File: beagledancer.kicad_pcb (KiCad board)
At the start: 2 copper layers, 40.6 x 29.2 mm, 12 parts, among them P9 BeagleBone, Q1 12MHz, U1 MAX3421

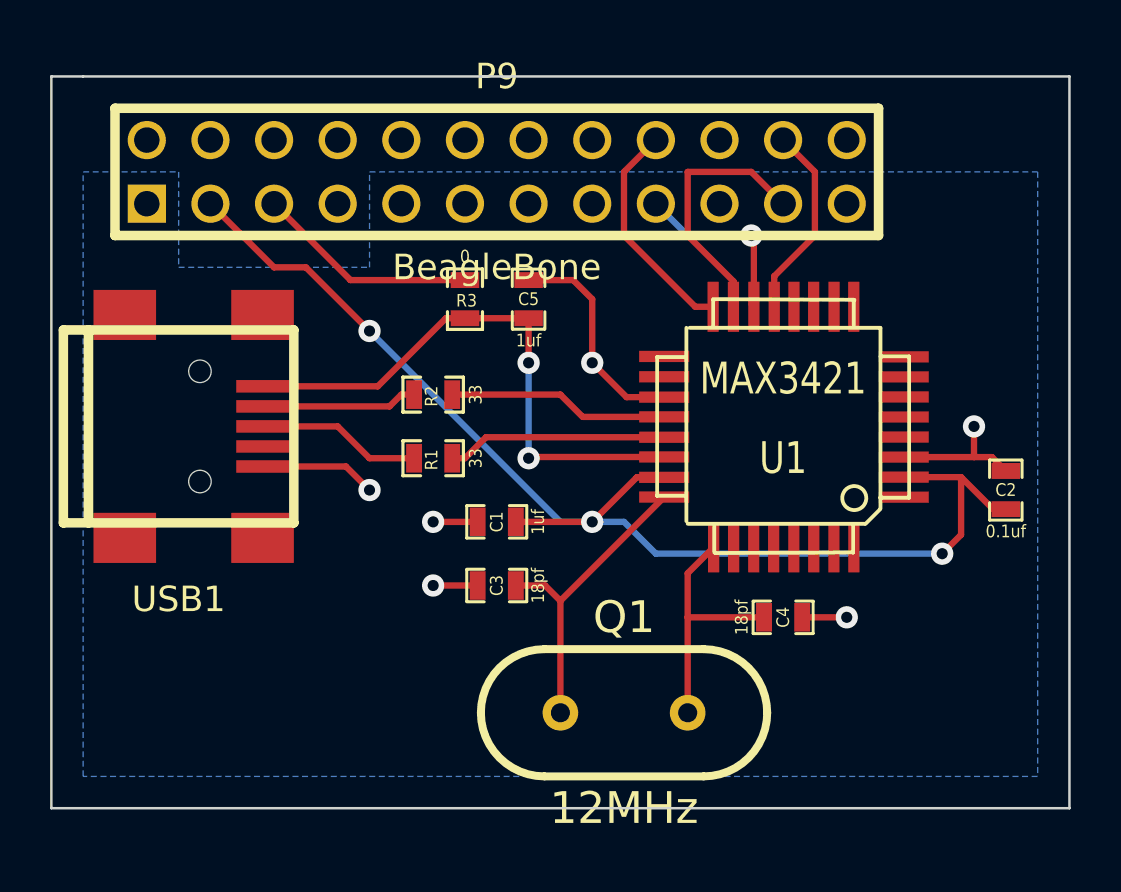
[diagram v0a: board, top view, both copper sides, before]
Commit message: Update based on feedback from Michael Ossmann (mossmann)
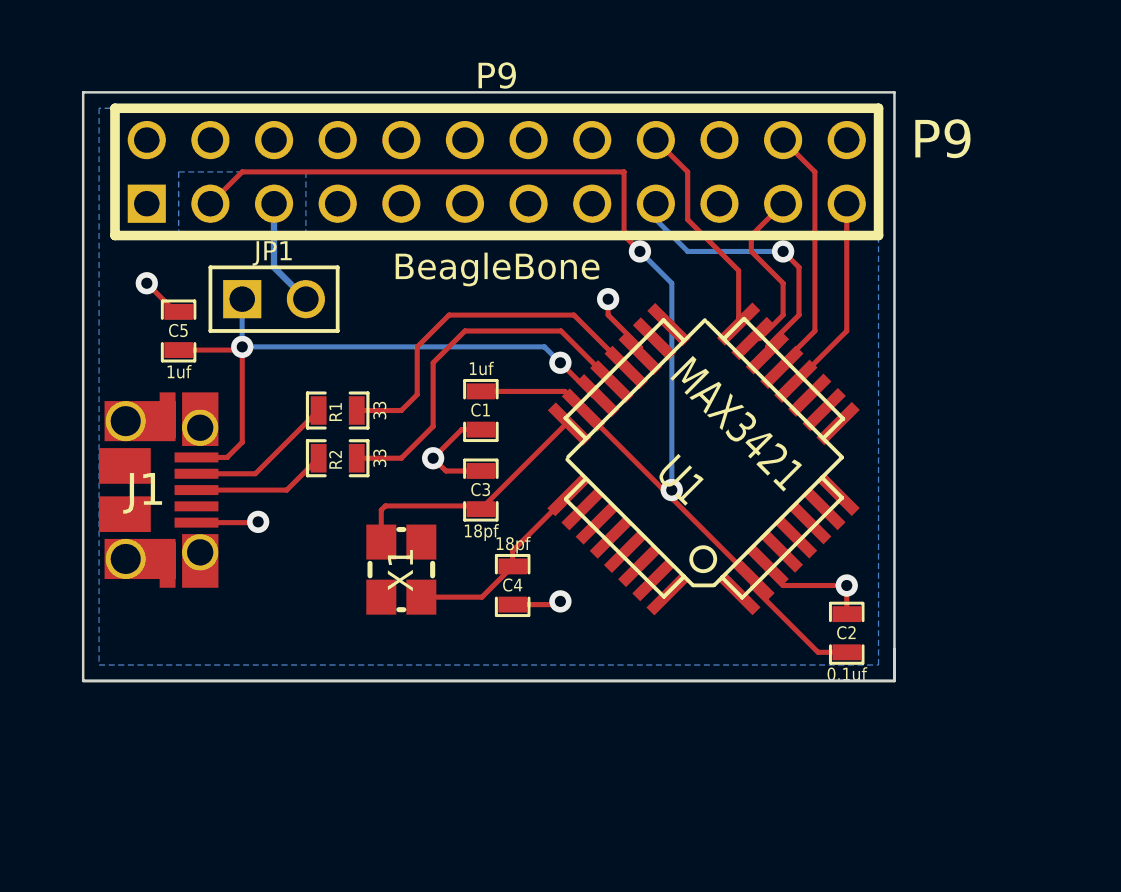
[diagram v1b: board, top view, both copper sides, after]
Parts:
- removed Q1: 12MHz, HC-49V
- removed R3: 0, SM0603_Resistor
- removed USB1: USB-MINI-B, USB_MINI_B
- added J1: USB-MICRO-B, GSG-USB-MICROB-FCI-10103594, F.Cu at (198.1, 152.4)
- added JP1: JUMPER, PIN_ARRAY_2X1, F.Cu at (205.7, 144.8)
- added X1: XTAL4PIN, GSG-XTAL3.2x2.5mm, F.Cu at (210.8, 155.6)
- moved C5 14.0 mm to (201.9, 146.1)
- moved C4 10.9 mm to (215.3, 156.2), turned to 270 degrees
- moved C2 8.54 mm to (228.6, 158.1)
- moved R2 4.58 mm to (208.3, 151.1)
- moved C1 4.49 mm to (214.0, 149.2), turned to 270 degrees
- moved R1 4.26 mm to (208.3, 149.2)
- moved C3 3.86 mm to (214.0, 152.4), turned to 90 degrees
- moved U1 3.42 mm to (222.9, 151.1), turned to 135 degrees
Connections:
- P9 pad 23: N-0000014 (its old number) -> N-0000038
- R1 pad 1: N-0000038 -> N-0000029
- R2 pad 1: N-0000029 -> N-0000027
- U1 pad 12: N-0000048 (its old number) -> N-0000038
- U1 pad 21: N-0000038 -> N-0000027
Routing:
- net N-0000027: track 0.00 -> 14.6 mm
- net GND: track 24.3 -> 18.1 mm
- net N-0000029: track 8.83 -> 14.3 mm
- net +5V: track 8.88 -> 4.34 mm
- net SPI0_CS0: track 7.37 -> 11.1 mm
- net SPI0_D0: track 10.5 -> 7.08 mm
- net N-0000049: track 22.7 -> 25.7 mm
- net SPI0_SCLK: track 7.85 -> 10.1 mm
- net N-000002: track 12.4 -> 10.2 mm
- net N-000003: track 10.1 -> 7.95 mm
- net N-0000038: track 8.81 -> 7.31 mm
- net N-0000025: track 6.14 -> 5.40 mm
- net N-0000022: track 6.47 -> 5.92 mm
- net +3.3V: track 49.6 -> 49.9 mm, vias 3 -> 2
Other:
- board size 40.6 x 29.2 mm -> 32.4 x 23.5 mm
- net class Default: clearance 0.254 -> 0.2032; trace_width 0.254 -> 0.2032
- rule trace_clearance: 0.254 -> 0.2032
- rule trace_min: 0.254 -> 0.2032
- board text added: "P9"

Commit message: Tweak layout to detect OTG pin status with GPIO pin
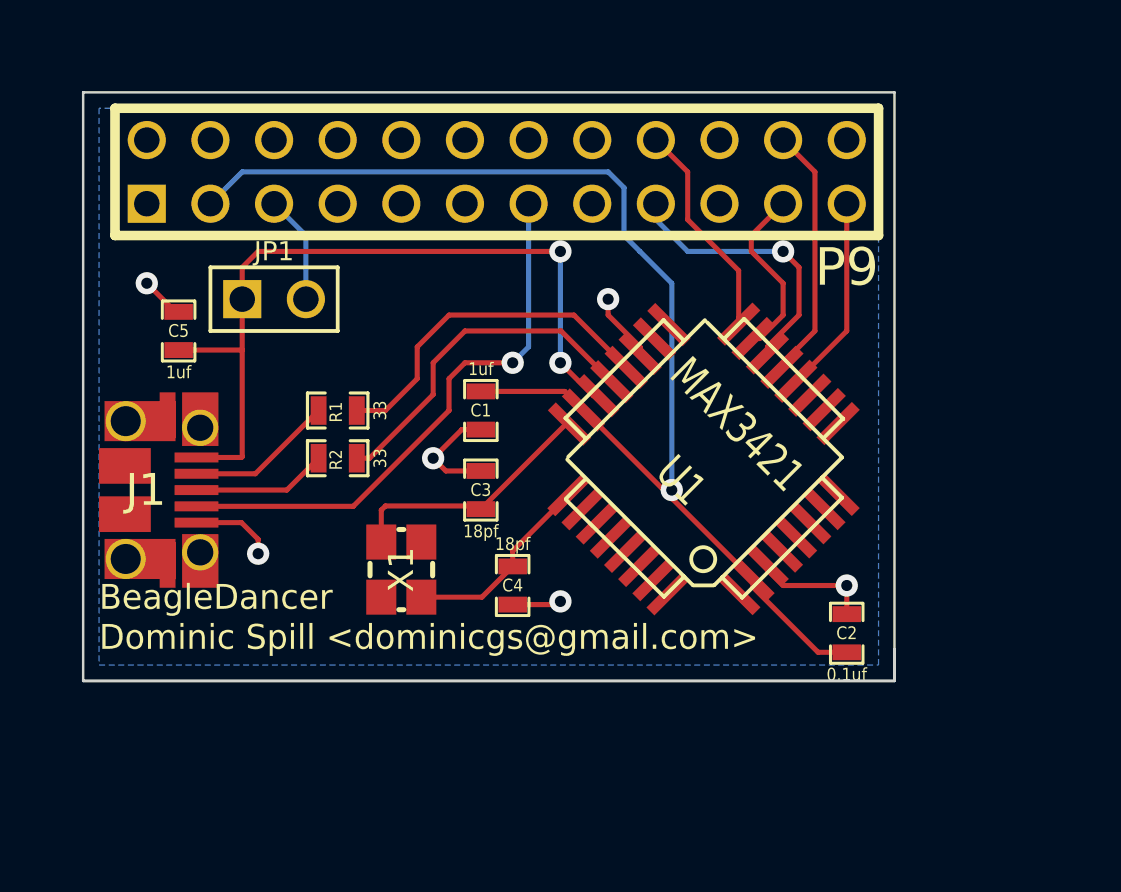
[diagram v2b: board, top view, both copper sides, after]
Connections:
- J1 pad 4: N-0000026 (its old number) -> USB_ID
- P9 pad 13: N-0000048 (its old number) -> USB_ID
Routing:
- net USB_ID: track 0.00 -> 22.4 mm, vias 0 -> 1
- net N-0000048: track 25.7 -> 31.6 mm
- net GND: track 18.1 -> 19.0 mm
- net N-0000025: track 14.6 -> 13.9 mm
- net +3.3V: track 49.9 -> 49.5 mm, vias 2 -> 1
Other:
- board text added: "BeagleDancer Dominic Spill <dominicgs@gmail.com>"

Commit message: More feedback
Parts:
- moved C3 4.84 mm to (209.6, 154.3), turned to 180 degrees
- moved X1 3.18 mm to (213.4, 153.7)
- moved C2 1.91 mm to (226.7, 158.1), turned to 0 degrees
- moved C4 1.42 mm to (216.5, 156.8), turned to 0 degrees
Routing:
- net GND: track 19.0 -> 13.7 mm, vias 6 -> 8
- net +3.3V: track 49.5 -> 48.3 mm, vias 1 -> 0
- net N-000002: track 10.2 -> 9.48 mm
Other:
- net class Default: via_dia 0.889 -> 1.016; via_drill 0.635 -> 0.508
- net class Power added: clearance 0.2032, trace_width 0.3048, via_dia 1.016, via_drill 0.508

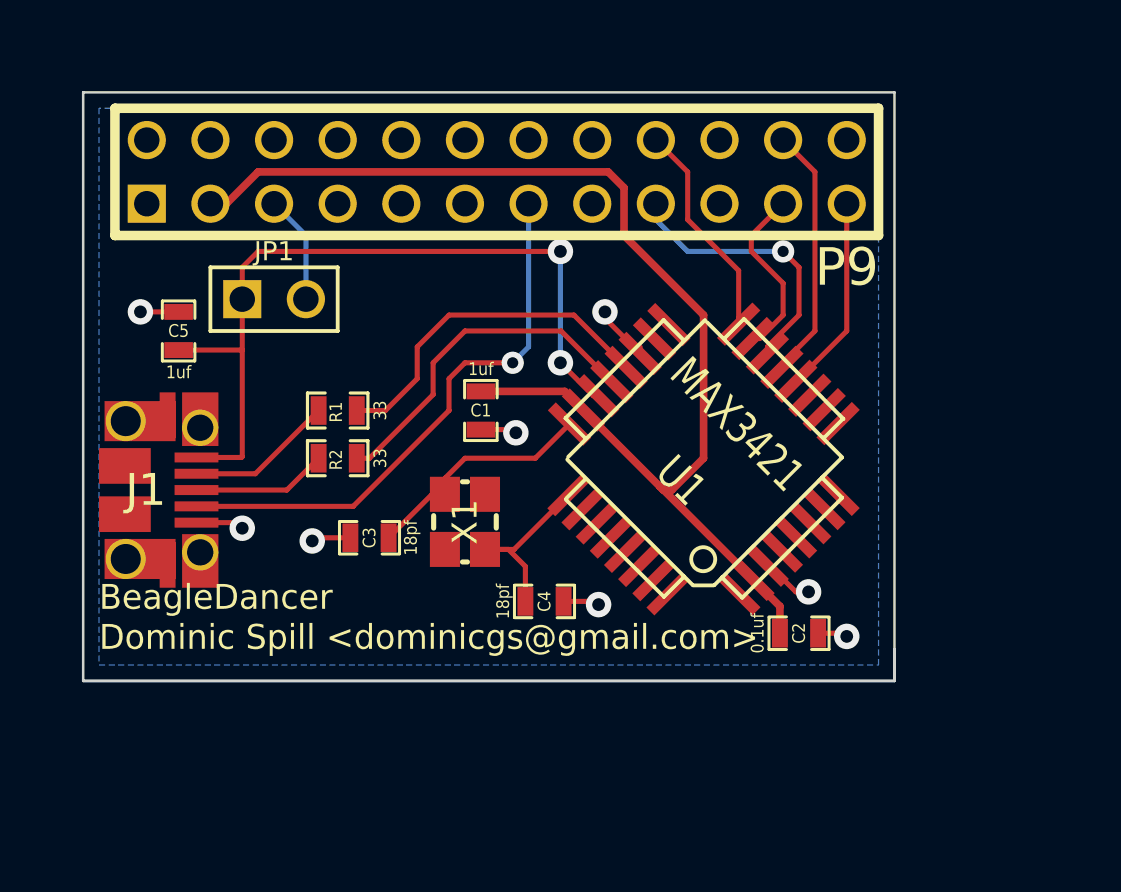
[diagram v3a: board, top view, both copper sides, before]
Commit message: Connect INT and GPX to GPIO pins on the Beagle.
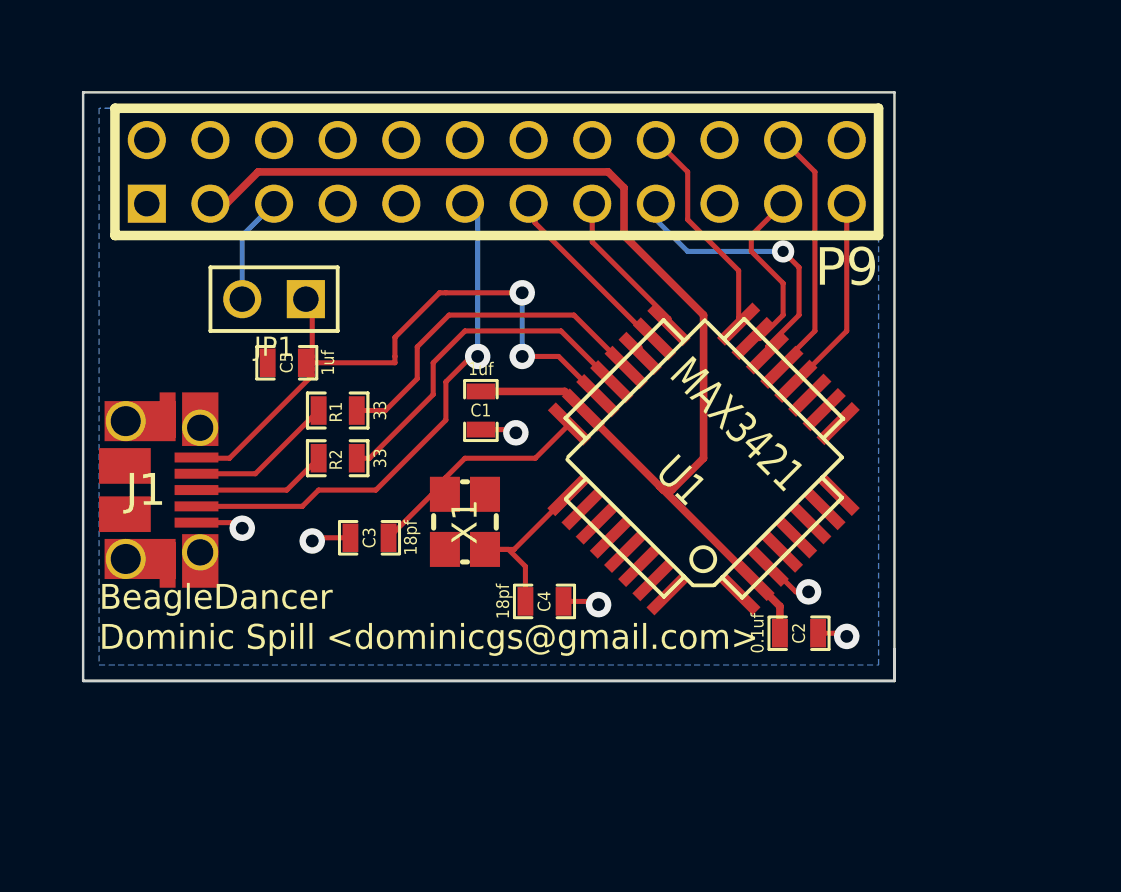
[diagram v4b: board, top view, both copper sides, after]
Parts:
- moved C5 4.50 mm to (206.2, 147.3), turned to 180 degrees
- turned JP1 to 180 degrees
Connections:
- P9 pad 11: N-0000030 (its old number) -> USB_ID
- P9 pad 13: USB_ID -> INT
- P9 pad 15: N-0000038 (its old number) -> GPX
- U1 pad 17: N-0000013 (its old number) -> GPX
- U1 pad 18: N-0000014 (its old number) -> INT
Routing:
- net INT: track 0.00 -> 7.56 mm
- net GPX: track 0.00 -> 6.09 mm
- net N-0000044: track 31.6 -> 26.8 mm
- net GND: track 13.7 -> 9.93 mm, vias 8 -> 6
- net USB_ID: track 22.4 -> 20.9 mm

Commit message: Fix MAX3421 size
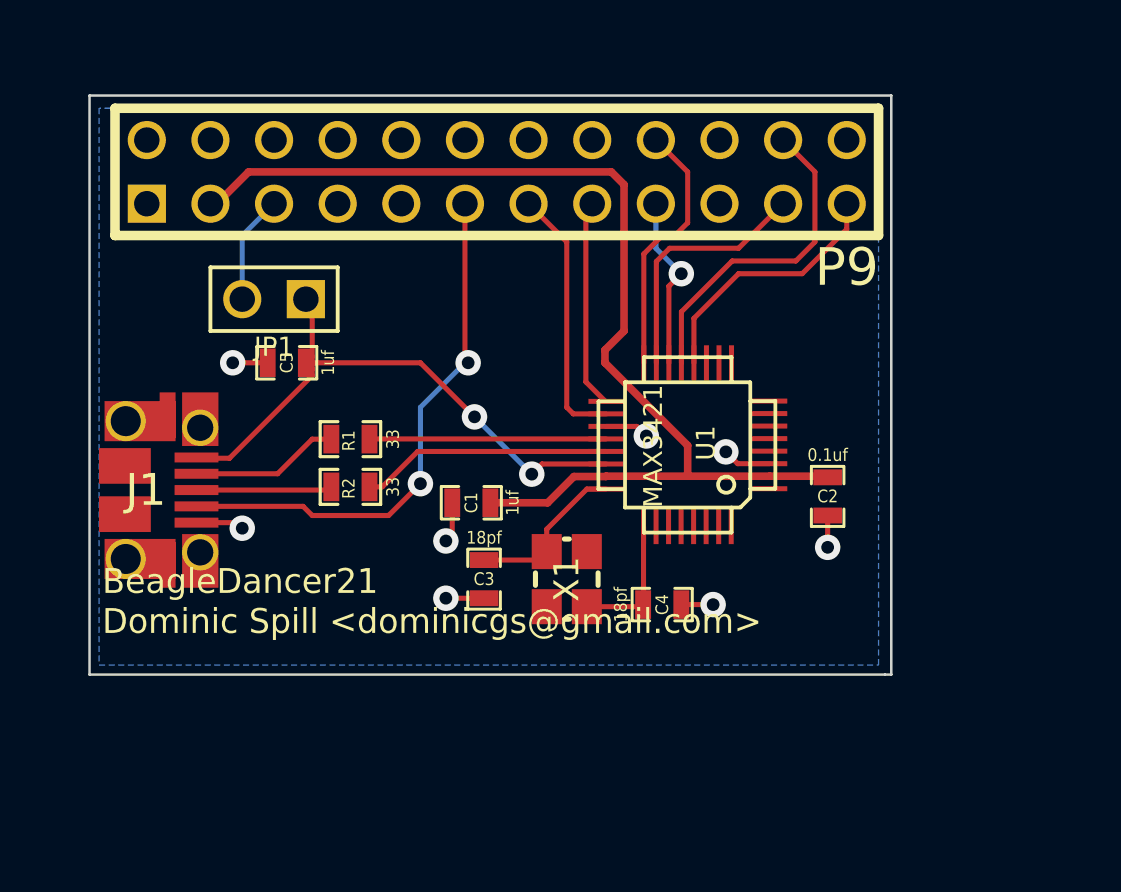
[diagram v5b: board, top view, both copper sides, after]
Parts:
- U1: footprint TQFP32 -> MAX3421
- moved C2 5.58 mm to (227.8, 152.7), turned to 270 degrees
- moved C3 4.86 mm to (214.1, 156.0), turned to 270 degrees
- moved C4 4.70 mm to (221.2, 157.0)
- moved X1 4.66 mm to (217.4, 156.0)
- moved C1 3.70 mm to (213.6, 152.9), turned to 180 degrees
- moved R1 1.25 mm to (208.8, 150.4)
- moved R2 1.25 mm to (208.8, 152.3)
- moved U1 0.81 mm to (222.2, 150.6), turned to 90 degrees
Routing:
- net N-0000026: track 13.9 -> 9.44 mm
- net N-0000025: track 13.9 -> 10.0 mm
- net +3.3V: track 48.3 -> 44.5 mm
- net SPI0_CS0: track 11.1 -> 7.61 mm
- net INT: track 7.56 -> 10.8 mm
- net N-0000033: track 7.31 -> 10.4 mm
- net SPI0_D0: track 7.08 -> 10.1 mm
- net SPI0_SCLK: track 10.1 -> 13.1 mm
- net N-0000044: track 26.8 -> 23.9 mm
- net GND: track 9.93 -> 12.7 mm, vias 6 -> 8
- net N-000002: track 9.48 -> 6.88 mm
- net GPX: track 6.09 -> 8.34 mm
- net N-000003: track 7.55 -> 5.40 mm
- net SPI0_D1: track 8.95 -> 10.4 mm
- net USB_ID: track 20.9 -> 21.7 mm, vias 1 -> 2
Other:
- board size 32.4 x 23.5 mm -> 32 x 23.1 mm
- board text added: "BeagleDancer21 Dominic Spill <dominicgs@gmail.com>"
- board text added: "https://github.com/dominicgs/BeagleDancer"
- board text removed: "BeagleDancer Dominic Spill <dominicgs@gmail.com>"
